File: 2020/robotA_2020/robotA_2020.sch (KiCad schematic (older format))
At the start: 14 parts, among them J1 UART_1, J2 I2C_3, J3 Motor_1, J4 Motor_2, J5 Encoder_1, J6 Encoder_2, J7 Encoder_M1, J8 Encoder_M2, U1 PCA9554D, U2 STM32L432KCUx

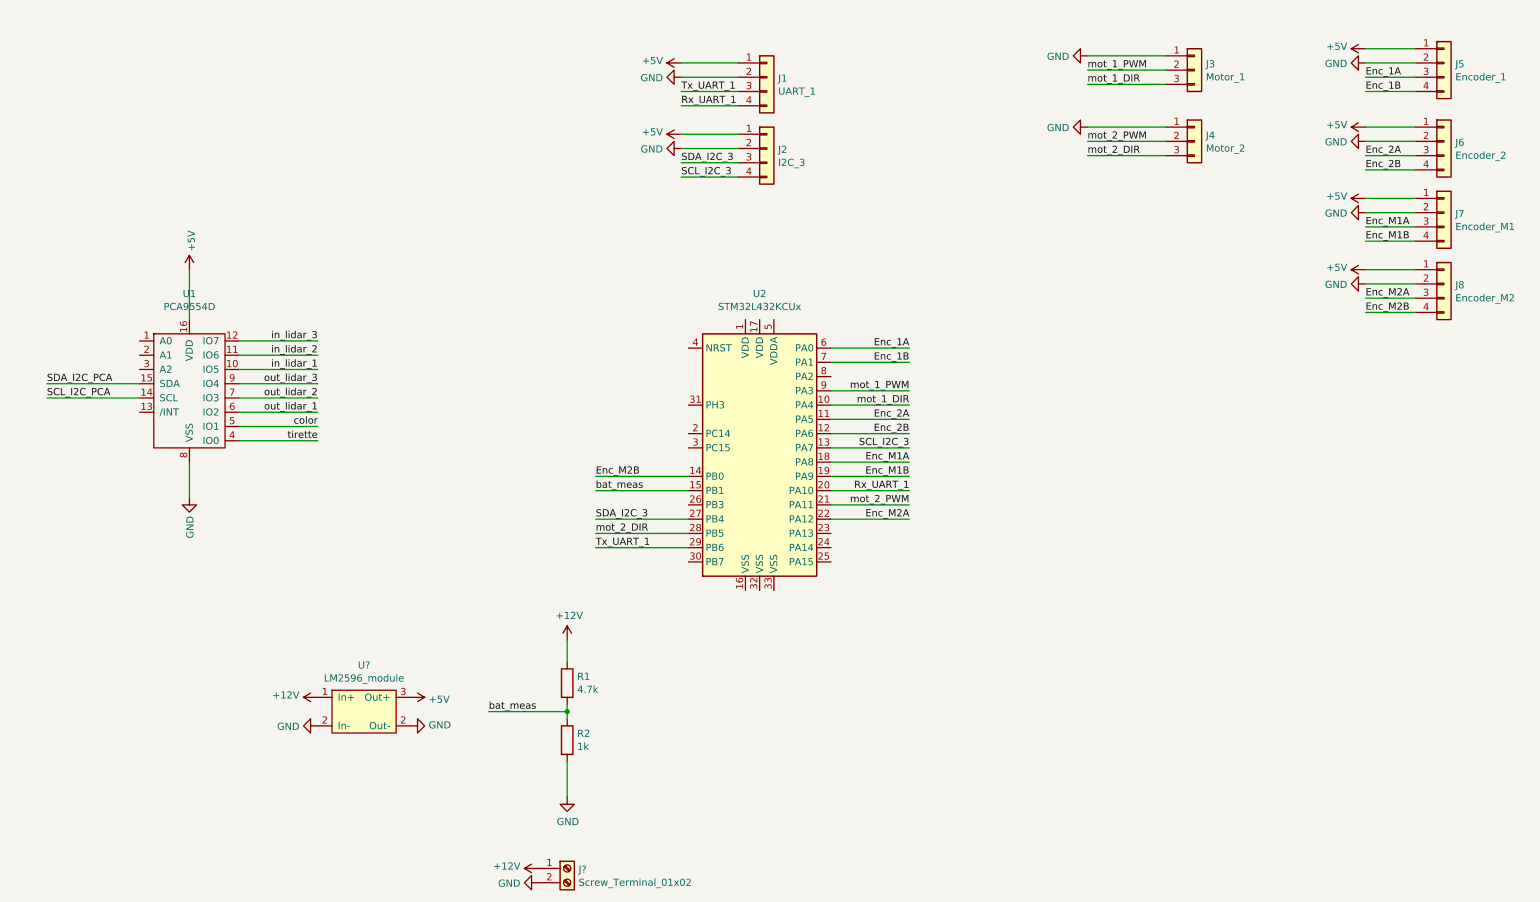
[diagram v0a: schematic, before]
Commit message: finish schematic PCA9685 and robotA
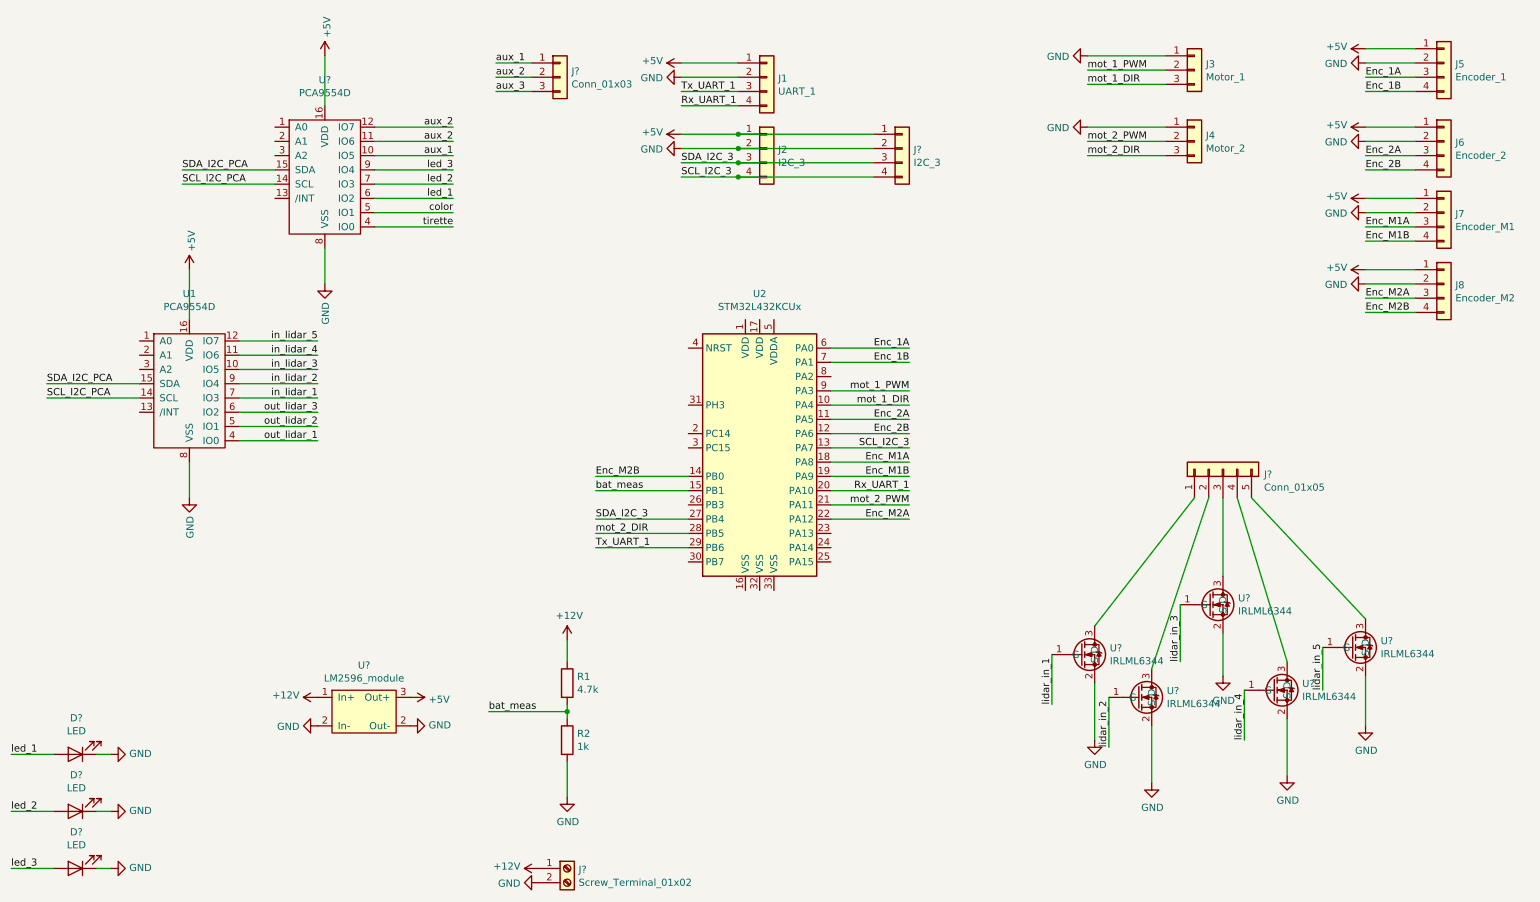
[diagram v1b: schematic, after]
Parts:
- added D? (x3): LED, LED_SMD:LED_0603_1608Metric, symbol Device:LED
- added J?: Conn_01x05, symbol Connector_Generic:Conn_01x05
- added J?: I2C_3, myFootprints:TerminalBlock_bornier-2_P5.08mm, symbol Connector_Generic:Conn_01x04
- added J?: Conn_01x03, symbol Connector_Generic:Conn_01x03
- added U?: PCA9554D, Package_SO:SSOP-16_5.3x6.2mm_P0.65mm, symbol mySymbols:PCA9554D
- added U? (x5): IRLML6344, myFootprints:SOT-23, symbol mySymbols:IRLML6344
- J1: footprint (none) -> Connector_JST:JST_EH_B4B-EH-A_1x04_P2.50mm_Vertical
- J2, J5, J6, J7, J8: footprint (none) -> myFootprints:TerminalBlock_bornier-2_P5.08mm
- J3, J4: footprint (none) -> Connector_JST:JST_EH_B3B-EH-A_1x03_P2.50mm_Vertical
- U1: footprint myFootprints:SOP-16_7.5x10.4mm_P1.27mm -> Package_SO:SSOP-16_5.3x6.2mm_P0.65mm
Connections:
- net +5V: now also J?.1 (Pin_1), U?.16 (VDD)
- net GND: now also D?.1 (K), D?.1 (K), D?.1 (K), J?.2 (Pin_2), U?.2 (S), U?.2 (S), U?.2 (S), U?.2 (S), U?.2 (S), U?.8 (VSS)
- net SCL_I2C_3: now also J?.4 (Pin_4)
- net SCL_I2C_PCA: now also U?.14 (SCL)
- net SDA_I2C_3: now also J?.3 (Pin_3)
- net SDA_I2C_PCA: now also U?.15 (SDA)
- net color: now also U?.5 (IO1); no longer U1.5 (IO1)
- net in_lidar_1: now also U1.7 (IO3); no longer U1.10 (IO5)
- net in_lidar_2: now also U1.9 (IO4); no longer U1.11 (IO6)
- net in_lidar_3: now also U1.10 (IO5); no longer U1.12 (IO7)
- net out_lidar_1: now also U1.4 (IO0); no longer U1.6 (IO2)
- net out_lidar_2: now also U1.5 (IO1); no longer U1.7 (IO3)
- net out_lidar_3: now also U1.6 (IO2); no longer U1.9 (IO4)
- net tirette: now also U?.4 (IO0); no longer U1.4 (IO0)
- new net: J?.1 (Pin_1), U?.3 (D)
- new net: J?.2 (Pin_2), U?.3 (D)
- new net: J?.3 (Pin_3), U?.3 (D)
- new net: J?.4 (Pin_4), U?.3 (D)
- new net: J?.5 (Pin_5), U?.3 (D)
- new net aux_1: J?.1 (Pin_1), U?.10 (IO5)
- new net aux_2: J?.2 (Pin_2), U?.11 (IO6), U?.12 (IO7)
- new net aux_3: J?.3 (Pin_3)
- new net in_lidar_4: U1.11 (IO6)
- new net in_lidar_5: U1.12 (IO7)
- new net led_1: D?.2 (A), U?.6 (IO2)
- new net led_2: D?.2 (A), U?.7 (IO3)
- new net led_3: D?.2 (A), U?.9 (IO4)
- new net lidar_in_1: U?.1 (G)
- new net lidar_in_2: U?.1 (G)
- new net lidar_in_3: U?.1 (G)
- new net lidar_in_4: U?.1 (G)
- new net lidar_in_5: U?.1 (G)

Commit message: Correction cartes 2020 robotA
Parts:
- removed U2: STM32L432KCUx, Package_DFN_QFN:QFN-32-1EP_5x5mm_P0.5mm_EP3.45x3.45mm, symbol MCU_ST_STM32L4:STM32L432KCUx
- added C1: 100nF, Capacitor_SMD:C_0603_1608Metric_Pad1.05x0.95mm_HandSolder, symbol Device:C
- added J13: Conn_01x03, Connector_JST:JST_EH_B3B-EH-A_1x03_P2.50mm_Vertical, symbol Connector_Generic:Conn_01x03
- added J14, J15: Conn_01x02, Connector_JST:JST_EH_B2B-EH-A_1x02_P2.50mm_Vertical, symbol Connector_Generic:Conn_01x02
- added U2: NUCLEO32-L432KC, myFootprints:NUCLEO32, symbol mySymbols:NUCLEO32-L432KC
- J11: renamed from J?; footprint myFootprints:TerminalBlock_bornier-2_P5.08mm -> Connector_JST:JST_EH_B4B-EH-A_1x04_P2.50mm_Vertical
- J12: renamed from J?; footprint (none) -> Connector_JST:JST_EH_B5B-EH-A_1x05_P2.50mm_Vertical
- J2, J5, J6, J7, J8: footprint myFootprints:TerminalBlock_bornier-2_P5.08mm -> Connector_JST:JST_EH_B4B-EH-A_1x04_P2.50mm_Vertical
- J9: renamed from J?; footprint (none) -> Connector_JST:JST_EH_B3B-EH-A_1x03_P2.50mm_Vertical
- gave numbers to parts that had none: 11
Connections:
- net SCL_I2C_PCA is gone; now on net SCL_I2C_3: U1.14 (SCL), U3.14 (SCL)
- net SDA_I2C_PCA is gone; now on net SDA_I2C_3: U1.15 (SDA), U3.15 (SDA)
- net in_lidar_1 is gone; now on net lidar_in_1: U1.7 (IO3)
- net in_lidar_2 is gone; now on net lidar_in_2: U1.9 (IO4)
- net in_lidar_3 is gone; now on net lidar_in_3: U1.10 (IO5)
- net in_lidar_4 is gone; now on net lidar_in_4: U1.11 (IO6)
- net in_lidar_5 is gone; now on net lidar_in_5: U1.12 (IO7)
- net +5V: now also C1.2, U2.27 (5V)
- net Enc_1A: now also U2.19 (PA00)
- net Enc_1B: now also U2.20 (PA01)
- net Enc_2A: now also U2.23 (PA05)
- net Enc_2B: now also U2.24 (PA06)
- net Enc_M1A: now also U2.12 (PA08)
- net Enc_M1B: now also U2.1 (PA09)
- net Enc_M2A: now also U2.5 (PA12)
- net Enc_M2B: now also U2.6 (PB00)
- net GND: now also C1.1, J14.2 (Pin_2), J15.2 (Pin_2), U2.29 (GND)
- net Rx_UART_1: now also U2.2 (PA10)
- net SCL_I2C_3: now also U2.25 (PA07)
- net SDA_I2C_3: now also U2.15 (PB04)
- net Tx_UART_1: now also U2.8 (PB06)
- net aux_2: no longer U3.12 (IO7)
- net aux_3: now also U3.12 (IO7)
- net bat_meas: now also U2.9 (PB01)
- net color: now also U3.9 (IO4), J14.1 (Pin_1); no longer U3.5 (IO1)
- net led_1: now also U3.5 (IO1); no longer U3.6 (IO2)
- net led_2: now also U3.6 (IO2); no longer U3.7 (IO3)
- net led_3: now also U3.7 (IO3); no longer U3.9 (IO4)
- net mot_1_DIR: now also U2.22 (PA04)
- net mot_1_PWM: now also U2.21 (PA03)
- net mot_2_DIR: now also U2.14 (PB05)
- net mot_2_PWM: now also U2.13 (PA11)
- net tirette: now also J15.1 (Pin_1)
- net out_lidar_1 renamed lidar_out_1
- net lidar_out_1: now also J13.1 (Pin_1)
- net out_lidar_2 renamed lidar_out_2
- net lidar_out_2: now also J13.2 (Pin_2)
- net out_lidar_3 renamed lidar_out_3
- net lidar_out_3: now also J13.3 (Pin_3)

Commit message: Fin carte elec 2020 robot-a
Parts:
- added J16: Conn_01x02, Connector_JST:JST_EH_B2B-EH-A_1x02_P2.50mm_Vertical, symbol Connector_Generic:Conn_01x02
- added R3, R4: 2.2k, Resistor_SMD:R_0805_2012Metric, symbol Device:R
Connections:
- net +5V: now also R3.1, R4.1
- net GND: now also J16.2 (Pin_2)
- net SCL_I2C_3: now also R4.2
- net SDA_I2C_3: now also R3.2
- net Tx_UART_2: now reaches U2.26 (PA02)
- net Tx_UART_2: now also J16.1 (Pin_1)
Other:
- moved on the sheet: C1
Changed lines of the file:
@@
 	5300 3350 5850 3350
-Wire Wire Line
-	5300 3250 5850 3250
 Wire Wire Line
 	5300 2850 5550 2850
@@
 Wire Wire Line
 	3750 4050 4400 4050
-Wire Wire Line
-	3750 4150 4400 4150
 Text Label 3750 4150 0    50   ~ 0
 SDA_I2C_3
@@
 L Device:C C1
 U 1 1 5E8563FA
-P 6350 2950
-F 0 "C1" H 6465 2996 50  0000 L CNN
-F 1 "100nF" H 6465 2905 50  0000 L CNN
-F 2 "Capacitor_SMD:C_0603_1608Metric_Pad1.05x0.95mm_HandSolder" H 6388 2800 50  0001 C CNN
-F 3 "~" H 6350 2950 50  0001 C CNN
-	1    6350 2950
+P 6350 2850
+F 0 "C1" H 6465 2896 50  0000 L CNN
+F 1 "100nF" H 6465 2805 50  0000 L CNN
+F 2 "Capacitor_SMD:C_0603_1608Metric_Pad1.05x0.95mm_HandSolder" H 6388 2700 50  0001 C CNN
+F 3 "~" H 6350 2850 50  0001 C CNN
+	1    6350 2850
 	1    0    0    -1
 $EndComp
-Wire Wire Line
-	5550 3150 6350 3150
-Wire Wire Line
-	6350 3150 6350 3100
-Wire Wire Line
-	5300 3050 5550 3050
-Wire Wire Line
-	5550 3150 5550 3050
-Connection ~ 5550 3050
-Wire Wire Line
-	5550 3050 5850 3050
 Wire Wire Line
 	6350 2700 5550 2700
@@
 	5550 2850 5850 2850
 Wire Wire Line
-	6350 2800 6350 2700
+	5300 3050 5550 3050
+Wire Wire Line
+	5550 3000 6350 3000
+Wire Wire Line
+	5550 3000 5550 3050
+Connection ~ 5550 3050
+Wire Wire Line
+	5550 3050 5850 3050
+Wire Wire Line
+	5300 3150 5850 3150
+Text Label 5850 3150 2    50   ~ 0
+Tx_UART_2
+$Comp
+L Connector_Generic:Conn_01x02 J16
+U 1 1 5E695FD0
+P 6950 850
+F 0 "J16" H 7030 842 50  0000 L CNN
+F 1 "Conn_01x02" H 7030 751 50  0000 L CNN
+F 2 "Connector_JST:JST_EH_B2B-EH-A_1x02_P2.50mm_Vertical" H 6950 850 50  0001 C CNN
+F 3 "~" H 6950 850 50  0001 C CNN
+	1    6950 850
+	1    0    0    -1
+$EndComp
+Wire Wire Line
+	6750 850  6350 850
+Text Label 6350 850  0    50   ~ 0
+Tx_UART_2
+$Comp
+L power:GND #PWR0123
+U 1 1 5E695FD8
+P 6750 950
+F 0 "#PWR0123" H 6750 700 50  0001 C CNN
+F 1 "GND" V 6755 822 50  0000 R CNN
+F 2 "" H 6750 950 50  0001 C CNN
+F 3 "" H 6750 950 50  0001 C CNN
+	1    6750 950
+	0    1    1    0
+$EndComp
+$Comp
+L Device:R R4
+U 1 1 5E6F05E5
+P 6500 3250
+F 0 "R4" V 6400 3250 50  0000 L CNN
+F 1 "2.2k" V 6600 3150 50  0000 L CNN
+F 2 "Resistor_SMD:R_0805_2012Metric" V 6430 3250 50  0001 C CNN
+F 3 "~" H 6500 3250 50  0001 C CNN
+	1    6500 3250
+	0    1    1    0
+$EndComp
+$Comp
+L power:+5V #PWR0124
+U 1 1 5E703B63
+P 6650 3250
+F 0 "#PWR0124" H 6650 3100 50  0001 C CNN
+F 1 "+5V" V 6665 3378 50  0000 L CNN
+F 2 "" H 6650 3250 50  0001 C CNN
+F 3 "" H 6650 3250 50  0001 C CNN
+	1    6650 3250
+	0    1    1    0
+$EndComp
+Wire Wire Line
+	5300 3250 6350 3250
+$Comp
+L Device:R R3
+U 1 1 5E72354F
+P 3450 4150
+F 0 "R3" V 3550 4100 50  0000 L CNN
+F 1 "2.2k" V 3350 4050 50  0000 L CNN
+F 2 "Resistor_SMD:R_0805_2012Metric" V 3380 4150 50  0001 C CNN
+F 3 "~" H 3450 4150 50  0001 C CNN
+	1    3450 4150
+	0    -1   -1   0
+$EndComp
+$Comp
+L power:+5V #PWR0125
+U 1 1 5E723555
+P 3300 4150
+F 0 "#PWR0125" H 3300 4000 50  0001 C CNN
+F 1 "+5V" V 3315 4278 50  0000 L CNN
+F 2 "" H 3300 4150 50  0001 C CNN
+F 3 "" H 3300 4150 50  0001 C CNN
+	1    3300 4150
+	0    -1   -1   0
+$EndComp
+Wire Wire Line
+	3600 4150 4400 4150
 $EndSCHEMATC
